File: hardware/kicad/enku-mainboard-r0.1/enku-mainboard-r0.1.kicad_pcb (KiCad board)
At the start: 4 copper layers, 54 x 94 mm, 124 parts, among them U1 ESP32-S3-WROOM-1-N16R8

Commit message: Route EPD switch node to VGH diode
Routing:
- net EPD_SW: track 11.8 -> 18.9 mm
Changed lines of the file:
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@@
   (via (at 54.0 42.2) (size 0.7) (drill 0.35) (layers "F.Cu" "B.Cu") (net 30))
   (segment (start 54.0 42.2) (end 54.4 42.9) (width 0.3) (layer "F.Cu") (net 30))
+  (segment (start 51.7 36.7) (end 49.8 36.7) (width 0.3) (layer "F.Cu") (net 30))
+  (segment (start 49.8 36.7) (end 47.8 34.7) (width 0.3) (layer "F.Cu") (net 30))
+  (segment (start 47.8 34.7) (end 46.0 33.15) (width 0.3) (layer "F.Cu") (net 30))
 )

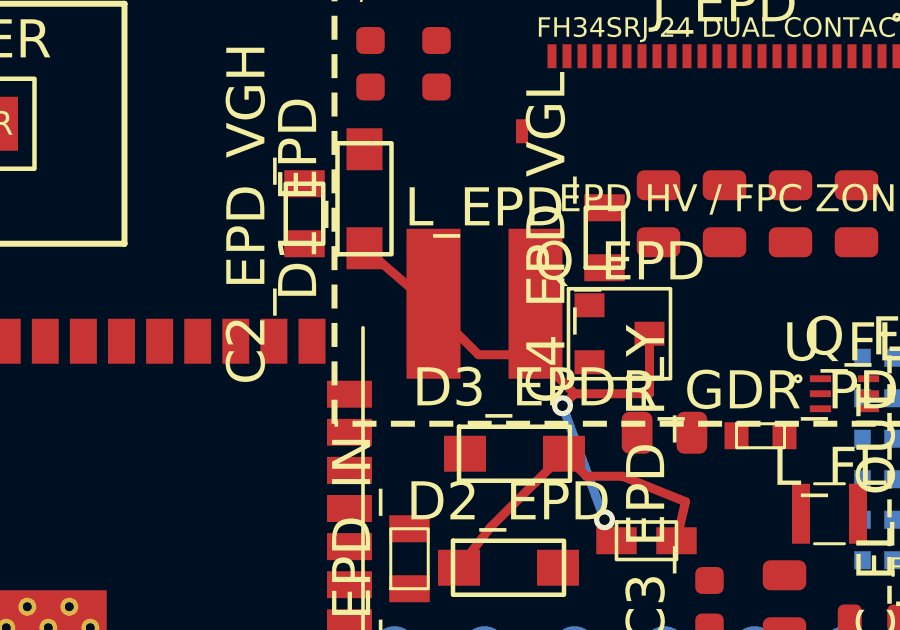
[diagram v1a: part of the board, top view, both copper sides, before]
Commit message: Route EPD switch diode branch below VCI inductor
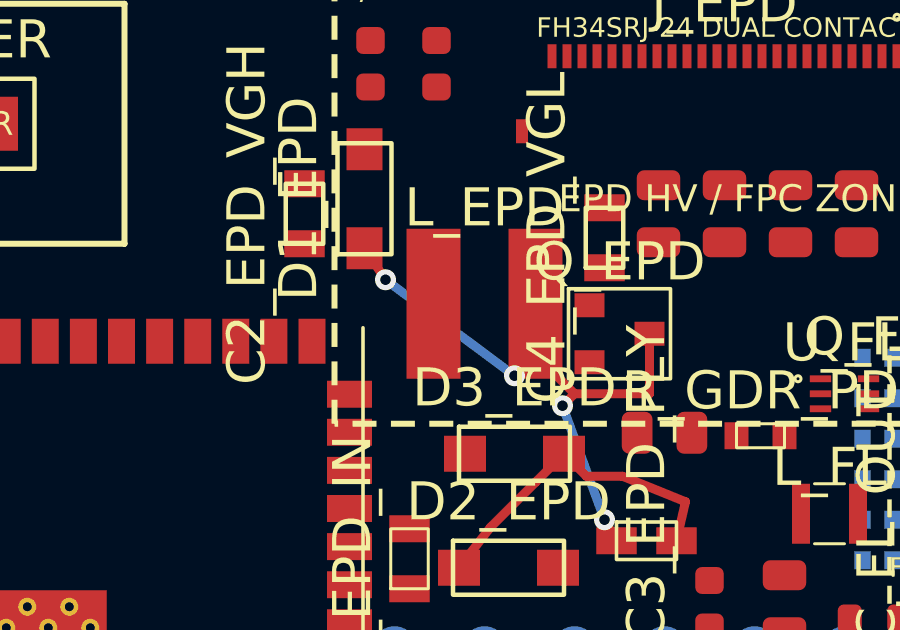
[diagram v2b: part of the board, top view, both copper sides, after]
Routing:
- net EPD_SW: track 18.9 -> 19.4 mm, vias 2 -> 4
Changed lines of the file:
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@@
   (via (at 54.0 42.2) (size 0.7) (drill 0.35) (layers "F.Cu" "B.Cu") (net 30))
   (segment (start 54.0 42.2) (end 54.4 42.9) (width 0.3) (layer "F.Cu") (net 30))
-  (segment (start 51.7 36.7) (end 49.8 36.7) (width 0.3) (layer "F.Cu") (net 30))
-  (segment (start 49.8 36.7) (end 47.8 34.7) (width 0.3) (layer "F.Cu") (net 30))
-  (segment (start 47.8 34.7) (end 46.0 33.15) (width 0.3) (layer "F.Cu") (net 30))
+  (segment (start 51.7 36.7) (end 51.0 37.4) (width 0.3) (layer "F.Cu") (net 30))
+  (via (at 51.0 37.4) (size 0.7) (drill 0.35) (layers "F.Cu" "B.Cu") (net 30))
+  (segment (start 51.0 37.4) (end 46.7 34.2) (width 0.3) (layer "B.Cu") (net 30))
+  (via (at 46.7 34.2) (size 0.7) (drill 0.35) (layers "F.Cu" "B.Cu") (net 30))
+  (segment (start 46.7 34.2) (end 46.0 33.15) (width 0.3) (layer "F.Cu") (net 30))
 )

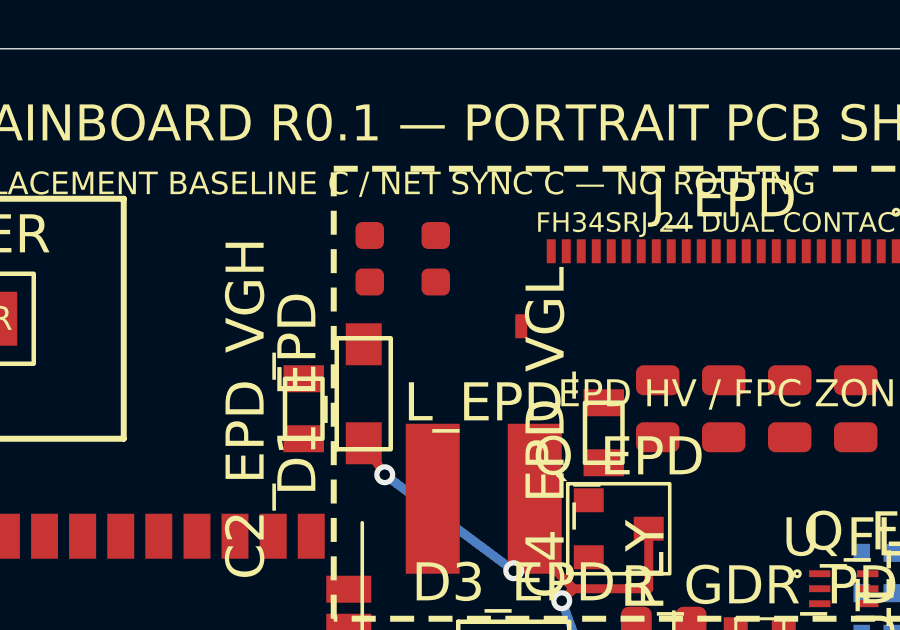
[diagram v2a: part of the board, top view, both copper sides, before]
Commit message: Route EPD VGH rail
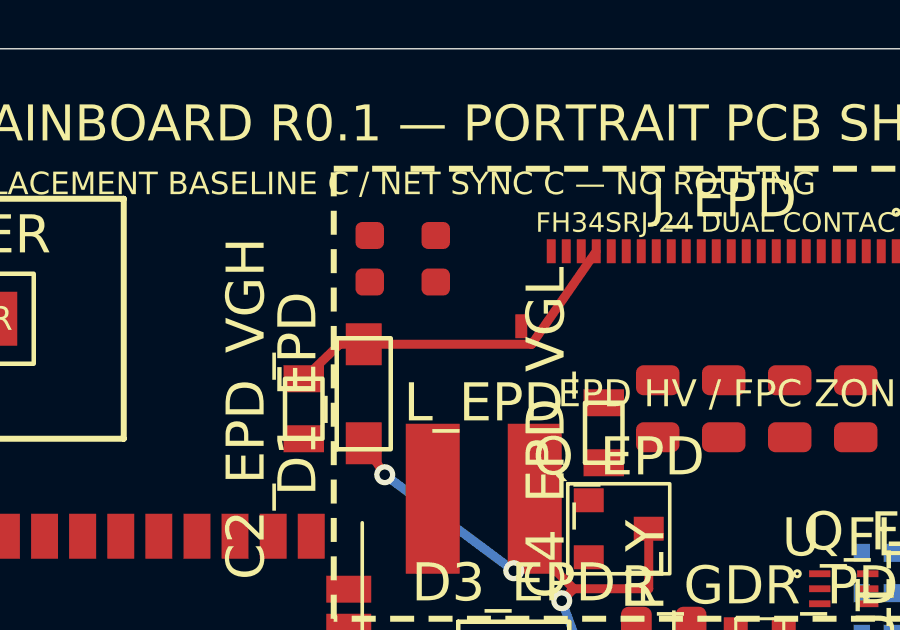
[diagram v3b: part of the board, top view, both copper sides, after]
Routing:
- net EPD_VGH: track 0.00 -> 11.8 mm
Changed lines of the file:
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@@
   (via (at 46.7 34.2) (size 0.7) (drill 0.35) (layers "F.Cu" "B.Cu") (net 30))
   (segment (start 46.7 34.2) (end 46.0 33.15) (width 0.3) (layer "F.Cu") (net 30))
+  (segment (start 46.0 29.85) (end 45.2 29.85) (width 0.3) (layer "F.Cu") (net 26))
+  (segment (start 45.2 29.85) (end 44.0 31.0) (width 0.3) (layer "F.Cu") (net 26))
+  (segment (start 46.0 29.85) (end 51.6 29.85) (width 0.3) (layer "F.Cu") (net 26))
+  (segment (start 51.6 29.85) (end 53.75 26.75) (width 0.3) (layer "F.Cu") (net 26))
 )

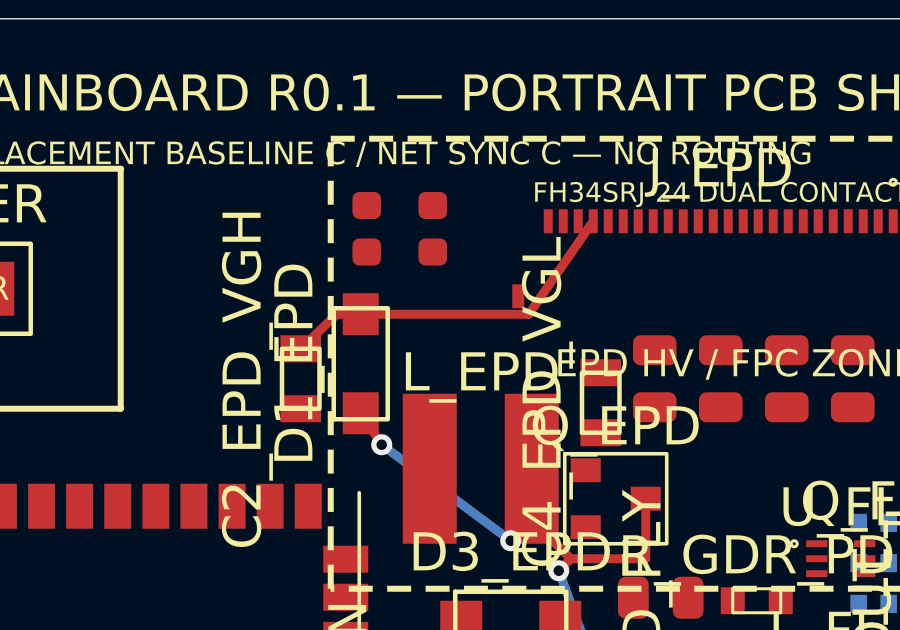
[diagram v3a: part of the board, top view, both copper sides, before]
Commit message: Correct EPD VGH pad routing
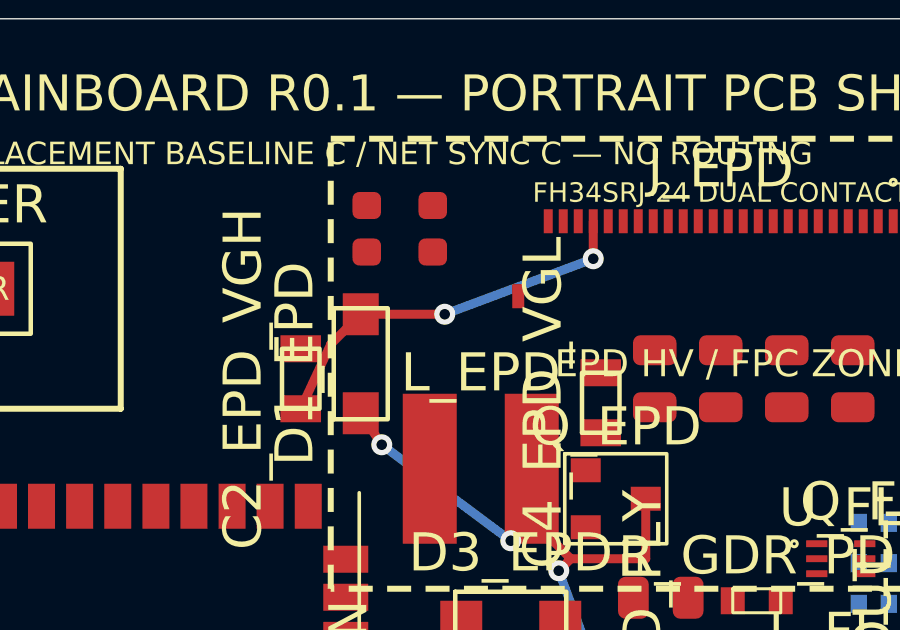
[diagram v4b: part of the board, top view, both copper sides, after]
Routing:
- net EPD_VGH: track 11.8 -> 13.1 mm, vias 0 -> 2
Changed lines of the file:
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@@
   (via (at 46.7 34.2) (size 0.7) (drill 0.35) (layers "F.Cu" "B.Cu") (net 30))
   (segment (start 46.7 34.2) (end 46.0 33.15) (width 0.3) (layer "F.Cu") (net 30))
-  (segment (start 46.0 29.85) (end 45.2 29.85) (width 0.3) (layer "F.Cu") (net 26))
-  (segment (start 45.2 29.85) (end 44.0 31.0) (width 0.3) (layer "F.Cu") (net 26))
-  (segment (start 46.0 29.85) (end 51.6 29.85) (width 0.3) (layer "F.Cu") (net 26))
-  (segment (start 51.6 29.85) (end 53.75 26.75) (width 0.3) (layer "F.Cu") (net 26))
+  (segment (start 46.0 29.85) (end 45.0 30.85) (width 0.3) (layer "F.Cu") (net 26))
+  (segment (start 45.0 30.85) (end 44.0 33.0) (width 0.3) (layer "F.Cu") (net 26))
+  (segment (start 46.0 29.85) (end 48.8 29.85) (width 0.3) (layer "F.Cu") (net 26))
+  (via (at 48.8 29.85) (size 0.7) (drill 0.35) (layers "F.Cu" "B.Cu") (net 26))
+  (segment (start 48.8 29.85) (end 53.75 28.0) (width 0.3) (layer "B.Cu") (net 26))
+  (via (at 53.75 28.0) (size 0.7) (drill 0.35) (layers "F.Cu" "B.Cu") (net 26))
+  (segment (start 53.75 28.0) (end 53.75 26.75) (width 0.3) (layer "F.Cu") (net 26))
 )

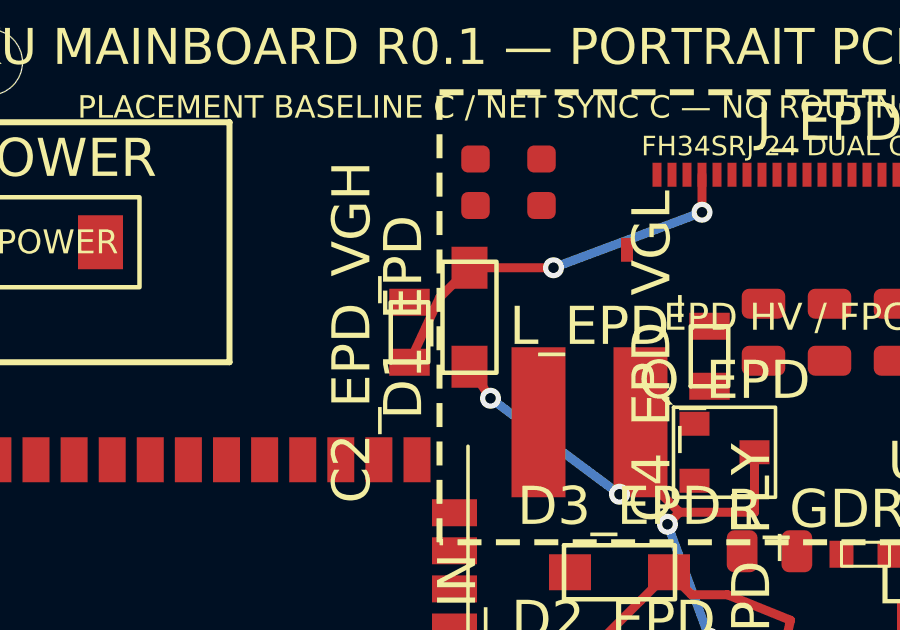
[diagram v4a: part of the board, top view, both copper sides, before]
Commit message: Route EPD VGH capacitor branch below ground pad
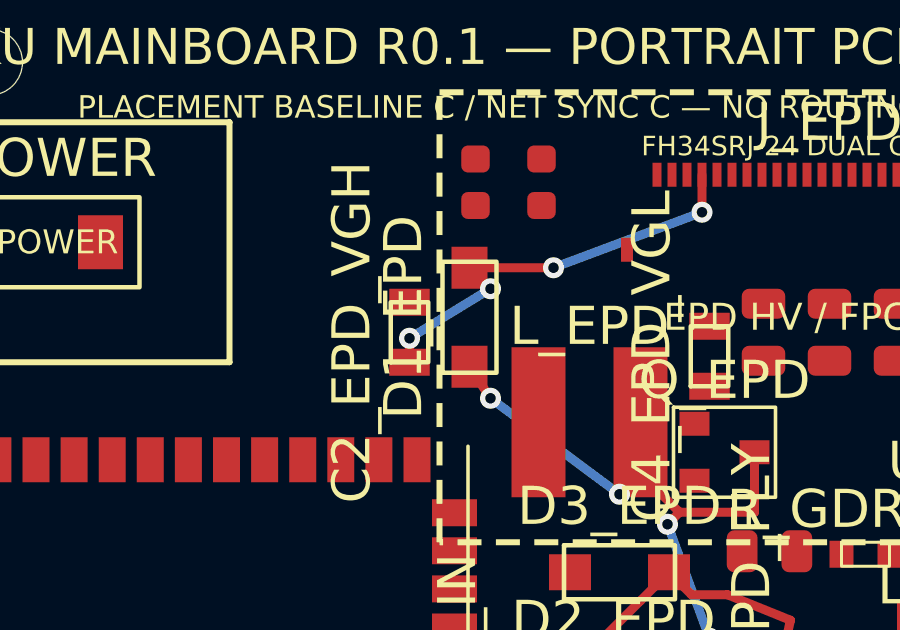
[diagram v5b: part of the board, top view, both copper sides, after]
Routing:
- net EPD_VGH: track 13.1 -> 14.3 mm, vias 2 -> 4
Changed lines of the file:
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@@
   (via (at 46.7 34.2) (size 0.7) (drill 0.35) (layers "F.Cu" "B.Cu") (net 30))
   (segment (start 46.7 34.2) (end 46.0 33.15) (width 0.3) (layer "F.Cu") (net 30))
-  (segment (start 46.0 29.85) (end 45.0 30.85) (width 0.3) (layer "F.Cu") (net 26))
-  (segment (start 45.0 30.85) (end 44.0 33.0) (width 0.3) (layer "F.Cu") (net 26))
   (segment (start 46.0 29.85) (end 48.8 29.85) (width 0.3) (layer "F.Cu") (net 26))
   (via (at 48.8 29.85) (size 0.7) (drill 0.35) (layers "F.Cu" "B.Cu") (net 26))
@@
   (via (at 53.75 28.0) (size 0.7) (drill 0.35) (layers "F.Cu" "B.Cu") (net 26))
   (segment (start 53.75 28.0) (end 53.75 26.75) (width 0.3) (layer "F.Cu") (net 26))
+  (segment (start 46.0 29.85) (end 46.7 30.55) (width 0.3) (layer "F.Cu") (net 26))
+  (via (at 46.7 30.55) (size 0.7) (drill 0.35) (layers "F.Cu" "B.Cu") (net 26))
+  (segment (start 46.7 30.55) (end 44.0 32.2) (width 0.3) (layer "B.Cu") (net 26))
+  (via (at 44.0 32.2) (size 0.7) (drill 0.35) (layers "F.Cu" "B.Cu") (net 26))
+  (segment (start 44.0 32.2) (end 44.0 33.0) (width 0.3) (layer "F.Cu") (net 26))
 )

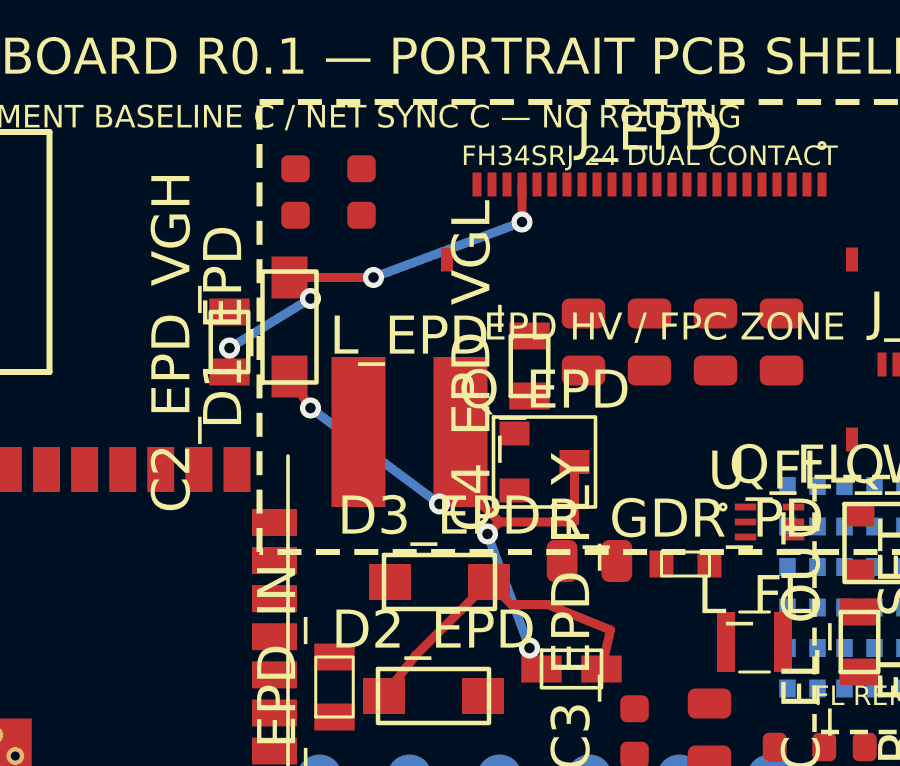
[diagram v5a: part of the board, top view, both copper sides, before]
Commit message: Route EPD VGL rail
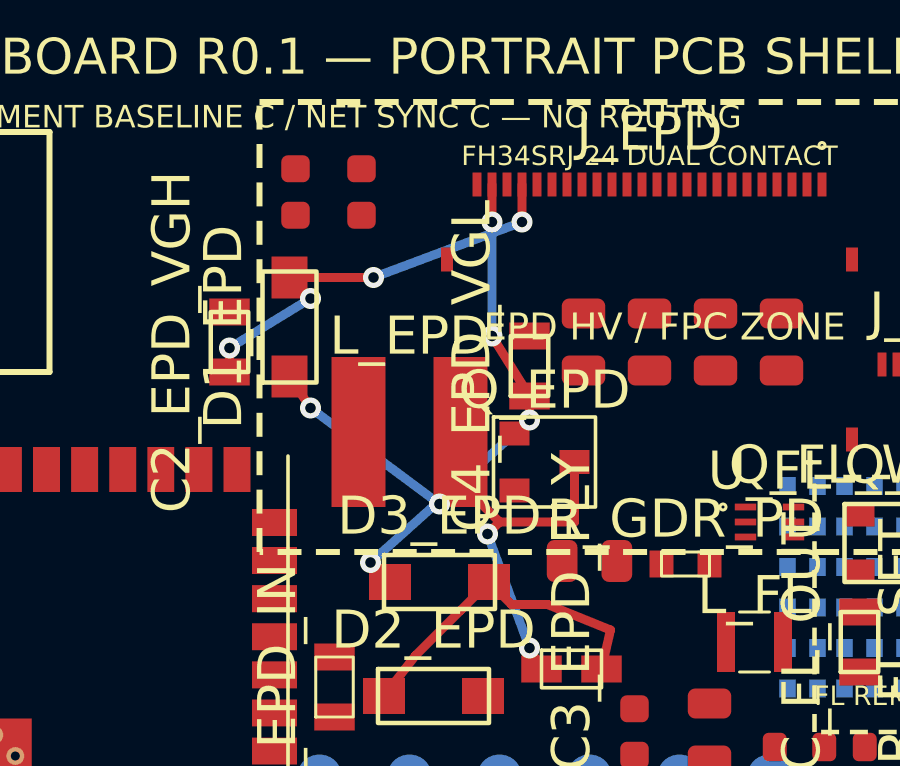
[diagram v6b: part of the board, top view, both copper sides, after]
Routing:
- net EPD_VGL: track 0.00 -> 16.2 mm, vias 0 -> 4
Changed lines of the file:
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@@
   (via (at 44.0 32.2) (size 0.7) (drill 0.35) (layers "F.Cu" "B.Cu") (net 26))
   (segment (start 44.0 32.2) (end 44.0 33.0) (width 0.3) (layer "F.Cu") (net 26))
+  (segment (start 49.35 40.0) (end 48.7 39.35) (width 0.3) (layer "F.Cu") (net 28))
+  (via (at 48.7 39.35) (size 0.7) (drill 0.35) (layers "F.Cu" "B.Cu") (net 28))
+  (segment (start 48.7 39.35) (end 54.0 34.6) (width 0.3) (layer "B.Cu") (net 28))
+  (via (at 54.0 34.6) (size 0.7) (drill 0.35) (layers "F.Cu" "B.Cu") (net 28))
+  (segment (start 54.0 34.6) (end 54.0 33.8) (width 0.3) (layer "F.Cu") (net 28))
+  (segment (start 54.0 33.8) (end 52.75 31.8) (width 0.3) (layer "F.Cu") (net 28))
+  (via (at 52.75 31.8) (size 0.7) (drill 0.35) (layers "F.Cu" "B.Cu") (net 28))
+  (segment (start 52.75 31.8) (end 52.75 28.0) (width 0.3) (layer "B.Cu") (net 28))
+  (via (at 52.75 28.0) (size 0.7) (drill 0.35) (layers "F.Cu" "B.Cu") (net 28))
+  (segment (start 52.75 28.0) (end 52.75 26.75) (width 0.3) (layer "F.Cu") (net 28))
 )
